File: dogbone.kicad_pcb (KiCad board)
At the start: 2 copper layers, 4.8 x 23 mm, 12 parts, among them M1 THRU_HOLE_PAD, M10 THRU_HOLE_PAD, M11 THRU_HOLE_PAD, M12 THRU_HOLE_PAD, M2 THRU_HOLE_PAD, M3 THRU_HOLE_PAD, M4 THRU_HOLE_PAD, M5 THRU_HOLE_PAD, M6 THRU_HOLE_PAD, M7 THRU_HOLE_PAD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

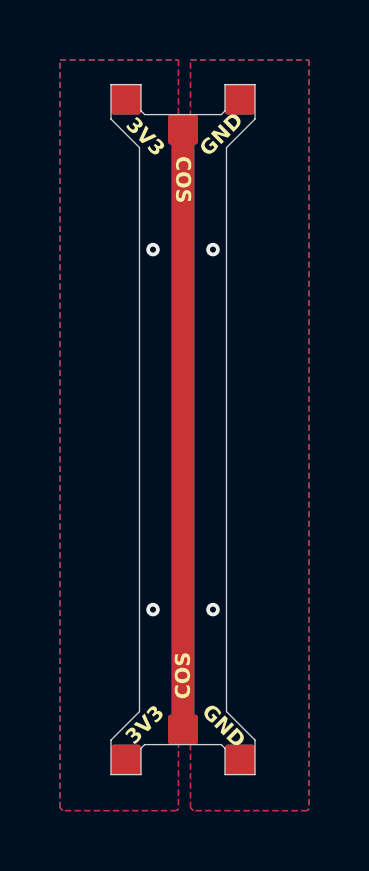
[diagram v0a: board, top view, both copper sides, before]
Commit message: net labelling, silkscreen, boards finished
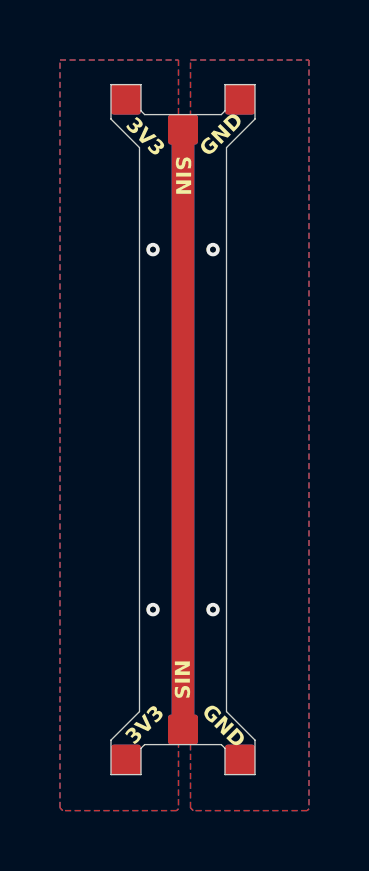
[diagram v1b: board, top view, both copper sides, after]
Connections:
- M2 pad 1: /COS -> /SIN
- M4 pad 1: /COS -> /SIN
- M6 pad 1: /SIN -> /COS
- M8 pad 1: /SIN -> /COS
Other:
- board text added: "SIN"
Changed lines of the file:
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@@
     )
     (pad "1" smd roundrect (at 0 0) (size 1 1) (layers "F.Cu" "F.Paste" "F.Mask") (roundrect_rratio 0.1)
-      (net 4 "/COS") (pinfunction "1") (pintype "passive") (thermal_bridge_angle 45))
+      (net 2 "/SIN") (pinfunction "1") (pintype "passive") (thermal_bridge_angle 45))
   )
   (footprint "adapter-encoder:dogbone_pad" (layer "F.Cu")
@@
     )
     (pad "1" smd roundrect (at 0 0) (size 1 1) (layers "F.Cu" "F.Paste" "F.Mask") (roundrect_rratio 0.1)
-      (net 4 "/COS") (pinfunction "1") (pintype "passive") (thermal_bridge_angle 45))
+      (net 2 "/SIN") (pinfunction "1") (pintype "passive") (thermal_bridge_angle 45))
   )
   (footprint "adapter-encoder:dogbone_pad" (layer "F.Cu")
@@
     )
     (pad "1" smd roundrect (at 0 0 180) (size 1 1) (layers "B.Cu" "B.Paste" "B.Mask") (roundrect_rratio 0.1)
-      (net 2 "/SIN") (pinfunction "1") (pintype "passive") (thermal_bridge_angle 45))
+      (net 4 "/COS") (pinfunction "1") (pintype "passive") (thermal_bridge_angle 45))
   )
   (footprint "adapter-encoder:dogbone_pad" (layer "B.Cu")
@@
     )
     (pad "1" smd roundrect (at 0 0 180) (size 1 1) (layers "B.Cu" "B.Paste" "B.Mask") (roundrect_rratio 0.1)
-      (net 2 "/SIN") (pinfunction "1") (pintype "passive") (thermal_bridge_angle 45))
+      (net 4 "/COS") (pinfunction "1") (pintype "passive") (thermal_bridge_angle 45))
   )
   (gr_line locked (start 86.12 47.59) (end 86.12 48.74)
@@
     (effects (font (size 0.5 0.5) (thickness 0.1) bold) (justify left bottom))
   )
-  (gr_text "COS" (at 88.23 49.97 -90) (layer "F.SilkS")
+  (gr_text "SIN" (at 88.23 49.97 270) (layer "F.SilkS")
     (effects (font (size 0.5 0.5) (thickness 0.1) bold) (justify left bottom))
   )
@@
     (effects (font (size 0.5 0.5) (thickness 0.1) bold) (justify left bottom))
   )
-  (gr_text "COS" (at 88.81 68.08 90) (layer "F.SilkS")
+  (gr_text "SIN" (at 88.81 68.08 90) (layer "F.SilkS")
     (effects (font (size 0.5 0.5) (thickness 0.1) bold) (justify left bottom))
   )
   (via (at 87.52 65.09) (size 0.45) (drill 0.2) (layers "F.Cu" "B.Cu") (free) (net 1))
   (via (at 87.52 53.09) (size 0.45) (drill 0.2) (layers "F.Cu" "B.Cu") (free) (net 1))
-  (segment (start 88.52 49.09) (end 88.52 69.09) (width 0.76) (layer "B.Cu") (net 2))
+  (segment (start 88.52 69.09) (end 88.52 49.09) (width 0.75) (layer "F.Cu") (net 2))
   (via (at 89.52 65.09) (size 0.45) (drill 0.2) (layers "F.Cu" "B.Cu") (free) (net 3))
   (via (at 89.52 53.09) (size 0.45) (drill 0.2) (layers "F.Cu" "B.Cu") (free) (net 3))
-  (segment (start 88.52 69.09) (end 88.52 49.09) (width 0.75) (layer "F.Cu") (net 4))
+  (segment (start 88.52 49.09) (end 88.52 69.09) (width 0.76) (layer "B.Cu") (net 4))
   (zone (net 1) (net_name "/+3V3") (layers "F&B.Cu") (hatch edge 0.5)
     (connect_pads yes (clearance 0.1524))
